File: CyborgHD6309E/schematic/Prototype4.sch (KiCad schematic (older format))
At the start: 21 parts, among them J1 Conn_AVR_UPDI, J2 Conn_AVR_UPDI, SW1 TSD1265, U1 ATmega4809-P, U2 HM628128DLP-5, U3 HD63C09E, U4 ATtiny412-SS, U5 CD74HCT30, U6 CD74HCT688

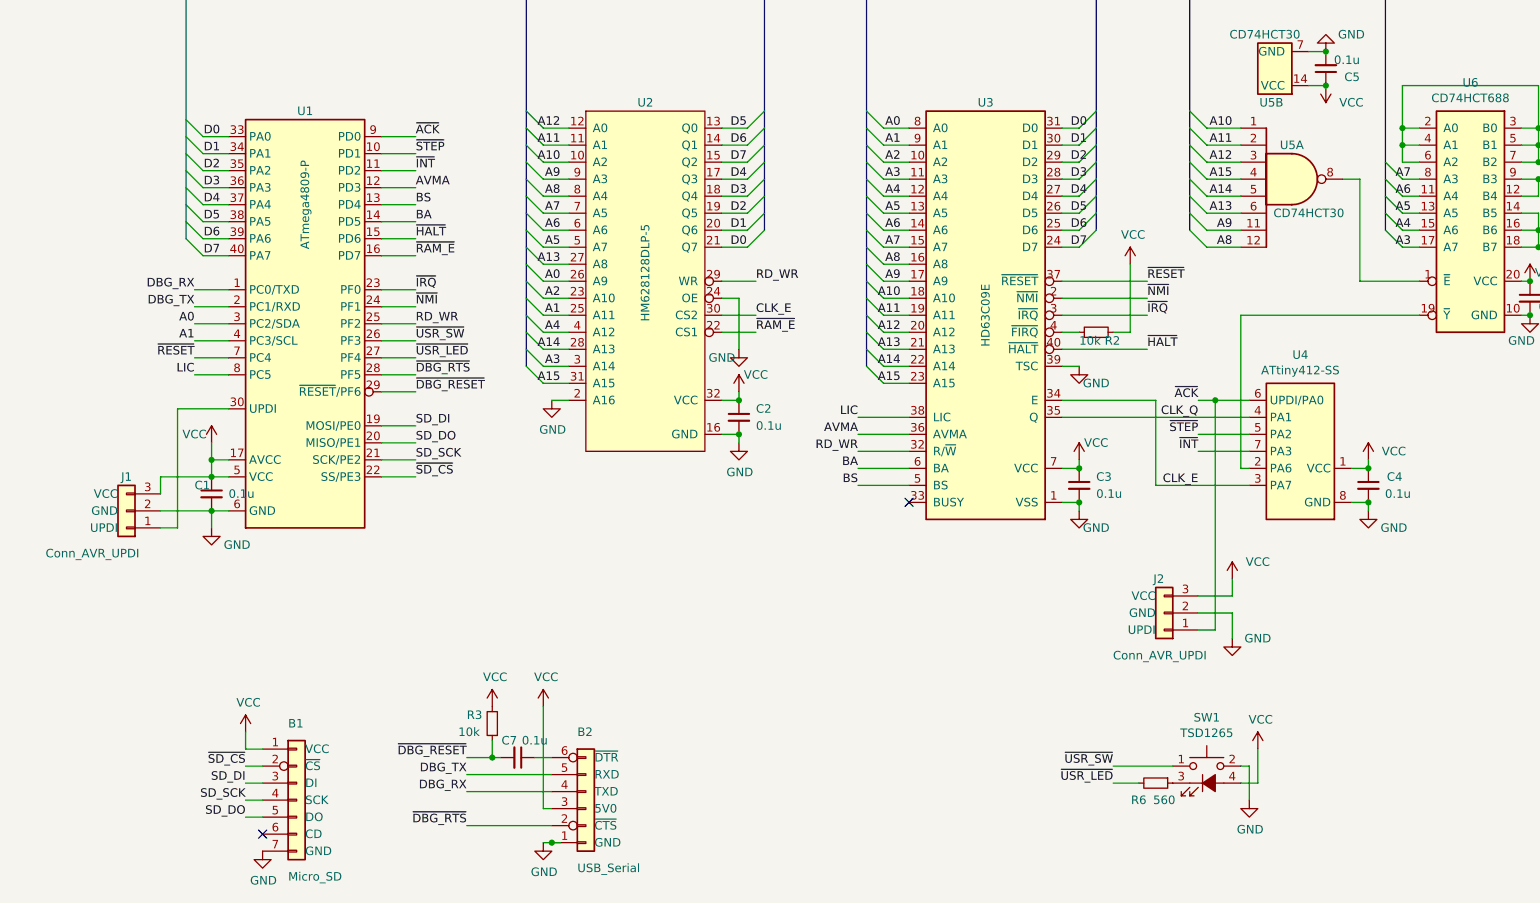
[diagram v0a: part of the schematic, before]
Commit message: [CyborgHD6309E] Update pins map
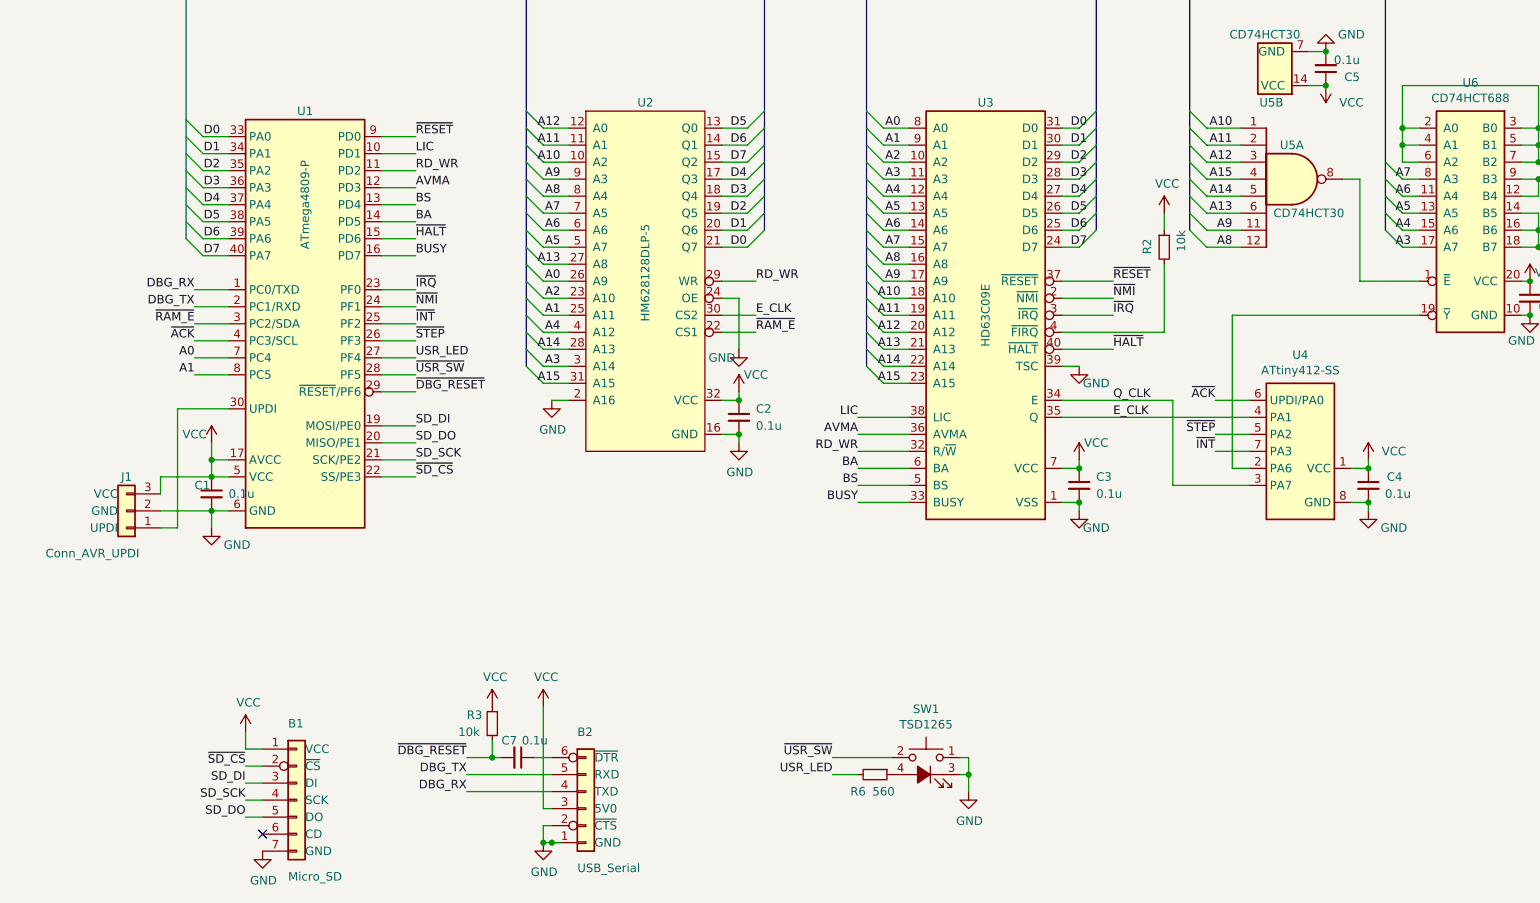
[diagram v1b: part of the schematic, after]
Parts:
- removed J2: Conn_AVR_UPDI, Connector_PinSocket_2.54mm:PinSocket_1x03_P2.54mm_Vertical, symbol 0-LocalLibrary:Conn_AVR_UPDI
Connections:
- net A0: now also U1.7 (PC4); no longer U1.3 (PC2/SDA)
- net A1: now also U1.8 (PC5); no longer U1.4 (PC3/SCL)
- net GND: now also B2.2 (~CTS~), SW1.1, SW1.3 (K); no longer SW1.2
- net LIC: now also U1.10 (PD1); no longer U1.8 (PC5)
- net RD_WR: now also U1.11 (PD2); no longer U1.25 (PF2)
- net VCC: now also R2.1; no longer R2.2, SW1.4 (A)
- net ~ACK~: now also U1.4 (PC3/SCL); no longer U1.9 (PD0)
- net ~INT~: now also U1.25 (PF2); no longer U1.11 (PD2)
- net ~RAM_E~: now also U1.3 (PC2/SDA); no longer U1.16 (PD7)
- net ~RESET~: now also U1.9 (PD0); no longer U1.7 (PC4)
- net ~STEP~: now also U1.26 (PF3); no longer U1.10 (PD1)
- net ~USR_SW~: now also SW1.2, U1.28 (PF5); no longer SW1.1, U1.26 (PF3)
- net BUSY: now reaches U3.33 (BUSY)
- net BUSY: now also U1.16 (PD7)
- net at U3.4 (~FIRQ): now also R2.2; no longer R2.1
- net at R6.1: now also SW1.4 (A); no longer SW1.3 (K)
- net CLK_E renamed Q_CLK
- net Q_CLK: no longer U2.30 (CS2)
- net CLK_Q renamed E_CLK
- net E_CLK: now also U2.30 (CS2)
- removed net ~DBG_RTS~: B2.2 (~CTS~), U1.28 (PF5)
- net ~USR_LED~ renamed USR_LED
- no-connect marks 2 -> 1
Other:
- moved on the sheet: R2, R6, SW1
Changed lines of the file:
@@
 Sheet 1 1
 Title "CyborgHD6309E Prototype4"
-Date "2020-12-29"
+Date "2021-01-29"
 Rev "4"
 Comp "Tadashi G. Takaoka"
@@
 	1    0    0    -1
 $EndComp
-NoConn ~ 6050 4250
 $Comp
 L power:GND #PWR08
@@
 F 3 "" H 3950 3650 50  0001 C CNN
 	1    3950 3650
-	1    0    0    -1
-$EndComp
-$Comp
-L power:VCC #PWR031
-U 1 1 5CE4D5BF
-P 7950 4700
-F 0 "#PWR031" H 7950 4550 50  0001 C CNN
-F 1 "VCC" H 8100 4800 50  0000 C CNN
-F 2 "" H 7950 4700 50  0001 C CNN
-F 3 "" H 7950 4700 50  0001 C CNN
-	1    7950 4700
-	1    0    0    -1
-$EndComp
-$Comp
-L power:GND #PWR032
-U 1 1 5CE4D62F
-P 7950 5050
-F 0 "#PWR032" H 7950 4800 50  0001 C CNN
-F 1 "GND" H 8100 5050 50  0000 C CNN
-F 2 "" H 7950 5050 50  0001 C CNN
-F 3 "" H 7950 5050 50  0001 C CNN
-	1    7950 5050
 	1    0    0    -1
 $EndComp
@@
 ~RAM_E~
 Text Label 5150 3150 0    50   ~ 0
-CLK_E
+E_CLK
 Text Label 5150 2950 0    50   ~ 0
 RD_WR
-Text Label 7750 4150 2    50   ~ 0
-CLK_E
-Text Label 7750 3750 2    50   ~ 0
-CLK_Q
+Text Label 7250 3750 0    50   ~ 0
+E_CLK
+Text Label 7250 3650 0    50   ~ 0
+Q_CLK
 Text Label 5750 3750 2    50   ~ 0
 LIC
@@
 Text Label 5750 4150 2    50   ~ 0
 BS
-Text Label 7750 3950 2    50   ~ 0
+Text Label 7850 3950 2    50   ~ 0
 ~INT~
-Text Label 7750 3650 2    50   ~ 0
+Text Label 7850 3650 2    50   ~ 0
 ~ACK~
-Text Label 7750 3850 2    50   ~ 0
+Text Label 7850 3850 2    50   ~ 0
 ~STEP~
 Text Label 3150 4100 0    50   ~ 0
 ~SD_CS~
-Text Label 1850 3300 2    50   ~ 0
+Text Label 1850 3500 2    50   ~ 0
 A1
-Text Label 1850 3200 2    50   ~ 0
+Text Label 1850 3400 2    50   ~ 0
 A0
 $Comp
@@
 $EndComp
 NoConn ~ 2250 6200
-Text Label 7250 5800 2    50   ~ 0
+Text Label 5600 5750 2    50   ~ 0
 ~USR_SW~
-Text Label 7250 5900 2    50   ~ 0
-~USR_LED~
+Text Label 5600 5850 2    50   ~ 0
+USR_LED
 $Comp
 L power:GND #PWR023
 U 1 1 5DD6FB12
-P 8050 6000
-F 0 "#PWR023" H 8050 5750 50  0001 C CNN
-F 1 "GND" H 8055 5827 50  0000 C CNN
-F 2 "" H 8050 6000 50  0001 C CNN
-F 3 "" H 8050 6000 50  0001 C CNN
-	1    8050 6000
+P 6400 5950
+F 0 "#PWR023" H 6400 5700 50  0001 C CNN
+F 1 "GND" H 6405 5777 50  0000 C CNN
+F 2 "" H 6400 5950 50  0001 C CNN
+F 3 "" H 6400 5950 50  0001 C CNN
+	1    6400 5950
 	1    0    0    -1
 $EndComp
@@
 Entry Wire Line
 	1800 2700 1900 2800
-Text Label 3450 6150 2    50   ~ 0
-~DBG_RTS~
-Wire Wire Line
-	3450 6150 3950 6150
 $Comp
 L 0-LocalLibrary:Conn_AVR_UPDI J1
@@
 $EndComp
 $Comp
-L 0-LocalLibrary:Conn_AVR_UPDI J2
-U 1 1 5EB45156
-P 7550 4800
-F 0 "J2" H 7550 4700 50  0000 L CNN
-F 1 "Conn_AVR_UPDI" H 7300 5150 50  0000 L CNN
-F 2 "Connector_PinSocket_2.54mm:PinSocket_1x03_P2.54mm_Vertical" H 7550 4800 50  0001 C CNN
-F 3 "~" H 7550 4800 50  0001 C CNN
-	1    7550 4800
-	-1   0    0    1
-$EndComp
-Wire Wire Line
-	7750 4800 7950 4800
-Wire Wire Line
-	7950 4800 7950 4700
-Wire Wire Line
-	7750 4900 7950 4900
-$Comp
 L power:VCC #PWR029
 U 1 1 5EC0C6A4
@@
 L 0-LocalLibrary:SW_Push_LED SW1
 U 1 1 5E9FC12A
-P 7800 5900
-F 0 "SW1" H 7800 6285 50  0000 C CNN
-F 1 "TSD1265" H 7800 6194 50  0000 C CNN
-F 2 "0-LocalLibrary:SW_PUSH-LED-12mm" H 7800 6200 50  0001 C CNN
-F 3 "~" H 7800 6200 50  0001 C CNN
-	1    7800 5900
-	1    0    0    -1
+P 6150 5850
+F 0 "SW1" H 6150 6235 50  0000 C CNN
+F 1 "TSD1265" H 6150 6144 50  0000 C CNN
+F 2 "0-LocalLibrary:SW_PUSH-LED-12mm" H 6150 6150 50  0001 C CNN
+F 3 "~" H 6150 6150 50  0001 C CNN
+	1    6150 5850
+	-1   0    0    -1
 $EndComp
 $Comp
 L Device:R_Small R6
 U 1 1 5DD95AB3
-P 7500 5900
-F 0 "R6" V 7600 5800 50  0000 C CNN
-F 1 "560" V 7600 5950 50  0000 C CNN
-F 2 "Resistor_THT:R_Axial_DIN0204_L3.6mm_D1.6mm_P5.08mm_Horizontal" H 7500 5900 50  0001 C CNN
-F 3 "~" H 7500 5900 50  0001 C CNN
-	1    7500 5900
+P 5850 5850
+F 0 "R6" V 5950 5750 50  0000 C CNN
+F 1 "560" V 5950 5900 50  0000 C CNN
+F 2 "Resistor_THT:R_Axial_DIN0204_L3.6mm_D1.6mm_P5.08mm_Horizontal" H 5850 5850 50  0001 C CNN
+F 3 "~" H 5850 5850 50  0001 C CNN
+	1    5850 5850
 	0    1    1    0
 $EndComp
 Wire Wire Line
-	8000 5800 8050 5800
+	6350 5750 6400 5750
 Wire Wire Line
 	3900 6250 3950 6250
@@
 $EndComp
 Wire Wire Line
-	8050 5800 8050 6000
-Wire Wire Line
-	8000 5900 8100 5900
-$Comp
-L power:VCC #PWR024
-U 1 1 5DD9AAAF
-P 8100 5700
-F 0 "#PWR024" H 8100 5550 50  0001 C CNN
-F 1 "VCC" H 8117 5873 50  0000 C CNN
-F 2 "" H 8100 5700 50  0001 C CNN
-F 3 "" H 8100 5700 50  0001 C CNN
-	1    8100 5700
-	1    0    0    -1
-$EndComp
-Wire Wire Line
-	8100 5700 8100 5900
-Wire Wire Line
-	7250 5900 7400 5900
-Wire Wire Line
-	7250 5800 7600 5800
+	6400 5750 6400 5850
+Wire Wire Line
+	5600 5850 5750 5850
+Wire Wire Line
+	5600 5750 5950 5750
 Wire Wire Line
 	2950 3000 3150 3000
@@
 	-1   0    0    -1
 $EndComp
-Wire Wire Line
-	8050 4150 7500 4150
-Wire Wire Line
-	7500 4150 7500 3650
-Wire Wire Line
-	7500 3650 6950 3650
-Wire Wire Line
-	6950 3750 8050 3750
-Wire Wire Line
-	7750 3850 8050 3850
-Wire Wire Line
-	7750 3950 8050 3950
-Wire Wire Line
-	7750 3650 7850 3650
-Wire Wire Line
-	7850 3650 7850 5000
-Wire Wire Line
-	7850 5000 7750 5000
-Connection ~ 7850 3650
-Wire Wire Line
-	7850 3650 8050 3650
-Wire Wire Line
-	7950 4900 7950 5050
 Connection ~ 7700 1250
 Wire Bus Line
@@
 	8700 2950 9050 2950
 Wire Wire Line
-	8050 4050 8000 4050
-Wire Wire Line
-	8000 4050 8000 3150
-Wire Wire Line
-	8000 3150 9050 3150
+	8050 4050 7950 4050
+Wire Wire Line
+	7950 4050 7950 3150
+Wire Wire Line
+	7950 3150 9050 3150
 Wire Wire Line
 	9050 2150 8950 2150
@@
 Wire Wire Line
 	2050 3400 1850 3400
-Text Label 1850 3400 2    50   ~ 0
+Text Label 3150 2100 0    50   ~ 0
 ~RESET~
 Wire Wire Line
 	2950 2300 3150 2300
-Text Label 3150 2300 0    50   ~ 0
-~INT~
 Wire Wire Line
 	2950 2100 3150 2100
-Text Label 3150 2100 0    50   ~ 0
+Text Label 1850 3300 2    50   ~ 0
 ~ACK~
 Wire Wire Line
 	2950 2200 3150 2200
-Text Label 3150 2200 0    50   ~ 0
-~STEP~
 Wire Wire Line
 	2950 2800 3150 2800
-Text Label 3150 2800 0    50   ~ 0
+Text Label 1850 3200 2    50   ~ 0
 ~RAM_E~
 Wire Wire Line
@@
 Wire Wire Line
 	2050 3500 1850 3500
-Text Label 1850 3500 2    50   ~ 0
+Text Label 3150 2200 0    50   ~ 0
 LIC
 Text Label 3150 3000 0    50   ~ 0
@@
 Text Label 3150 3600 0    50   ~ 0
 ~DBG_RESET~
-Text Label 3150 3300 0    50   ~ 0
+Text Label 3150 3500 0    50   ~ 0
 ~USR_SW~
 Text Label 3150 3400 0    50   ~ 0
-~USR_LED~
+USR_LED
 Wire Wire Line
 	2950 2500 3150 2500
@@
 Text Label 3150 2600 0    50   ~ 0
 BA
-Text Label 3150 3200 0    50   ~ 0
+Text Label 3150 2300 0    50   ~ 0
 RD_WR
-Text Label 7450 3150 0    50   ~ 0
+Text Label 7250 3150 0    50   ~ 0
 ~IRQ~
-Text Label 7450 2950 0    50   ~ 0
+Text Label 7250 2950 0    50   ~ 0
 ~RESET~
-Text Label 7450 3350 0    50   ~ 0
+Text Label 7250 3350 0    50   ~ 0
 ~HALT~
-Text Label 7450 3050 0    50   ~ 0
+Text Label 7250 3050 0    50   ~ 0
 ~NMI~
-Wire Wire Line
-	7450 2950 6950 2950
-Wire Wire Line
-	7450 3150 6950 3150
-Wire Wire Line
-	7450 3350 6950 3350
-Wire Wire Line
-	6950 3050 7450 3050
-Wire Wire Line
-	6950 3250 7050 3250
-Wire Wire Line
-	7350 2850 7350 3250
-Wire Wire Line
-	7250 3250 7350 3250
 $Comp
 L power:VCC #PWR022
 U 1 1 5CE72E6F
-P 7350 2850
-F 0 "#PWR022" H 7350 2700 50  0001 C CNN
-F 1 "VCC" H 7367 3023 50  0000 C CNN
-F 2 "" H 7350 2850 50  0001 C CNN
-F 3 "" H 7350 2850 50  0001 C CNN
-	1    7350 2850
+P 7550 2550
+F 0 "#PWR022" H 7550 2400 50  0001 C CNN
+F 1 "VCC" H 7567 2723 50  0000 C CNN
+F 2 "" H 7550 2550 50  0001 C CNN
+F 3 "" H 7550 2550 50  0001 C CNN
+	1    7550 2550
 	1    0    0    -1
 $EndComp
@@
 L Device:R_Small R2
 U 1 1 5D0B1917
-P 7150 3250
-F 0 "R2" V 7100 3200 50  0000 R CNN
-F 1 "10k" V 7100 3350 50  0000 R CNN
-F 2 "Resistor_THT:R_Axial_DIN0204_L3.6mm_D1.6mm_P5.08mm_Horizontal" H 7150 3250 50  0001 C CNN
-F 3 "" H 7150 3250 50  0001 C CNN
-	1    7150 3250
-	0    -1   -1   0
-$EndComp
-Text Label 3150 3500 0    50   ~ 0
-~DBG_RTS~
+P 7550 2750
+F 0 "R2" V 7450 2800 50  0000 R CNN
+F 1 "10k" V 7650 2850 50  0000 R CNN
+F 2 "Resistor_THT:R_Axial_DIN0204_L3.6mm_D1.6mm_P5.08mm_Horizontal" H 7550 2750 50  0001 C CNN
+F 3 "" H 7550 2750 50  0001 C CNN
+	1    7550 2750
+	1    0    0    -1
+$EndComp
+Wire Wire Line
+	6350 5850 6400 5850
+Connection ~ 6400 5850
+Wire Wire Line
+	6400 5850 6400 5950
+Text Label 3150 2800 0    50   ~ 0
+BUSY
+Wire Wire Line
+	6050 4250 5750 4250
+Text Label 5750 4250 2    50   ~ 0
+BUSY
+Wire Wire Line
+	3950 6150 3900 6150
+Wire Wire Line
+	3900 6150 3900 6250
+Connection ~ 3900 6250
+Text Label 3150 3200 0    50   ~ 0
+~INT~
+Text Label 3150 3300 0    50   ~ 0
+~STEP~
+Wire Wire Line
+	6950 3750 8050 3750
+Wire Wire Line
+	8050 3650 7850 3650
+Wire Wire Line
+	8050 3850 7850 3850
+Wire Wire Line
+	8050 3950 7850 3950
+Wire Wire Line
+	7600 3650 7600 4150
+Wire Wire Line
+	7600 4150 8050 4150
+Wire Wire Line
+	6950 3650 7600 3650
+Wire Wire Line
+	7550 2550 7550 2650
+Wire Wire Line
+	6950 2950 7250 2950
+Wire Wire Line
+	6950 3050 7250 3050
+Wire Wire Line
+	6950 3150 7250 3150
+Wire Wire Line
+	6950 3350 7250 3350
+Wire Wire Line
+	6950 3250 7550 3250
+Wire Wire Line
+	7550 3250 7550 2850
 Wire Bus Line
 	8850 1250 8850 2650
